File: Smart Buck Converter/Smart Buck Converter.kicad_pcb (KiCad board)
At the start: 2 copper layers, 80 x 45 mm, 73 parts, among them J1 691101710003, J2 PJ-063AH, J3 USB4105-GF-A, J4 PJ-063AH, J6 PJ-063AH, Q1 IRFR9220TRPBF-BE3, U1 LM2596S-ADJ, U2 ATSAMD21E18A-A, U3 AP2204K-3.3, U4 INA219AxD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

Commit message: Changes to README & Design
Updated revision number of hardware design to 2.0.0, despite the changes for this revision being implemented before this project was version controlled on GitHub. Also regenerated 3D view images of revision 2 and replaced them in the README. Added detail regarding known hardware bug in README.
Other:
- board text added: "Intelligent DC-DC Converter 04/2023 V2.0.0"
- board text removed: "Intelligent DC-DC Converter 03/2023 V1.0.0"

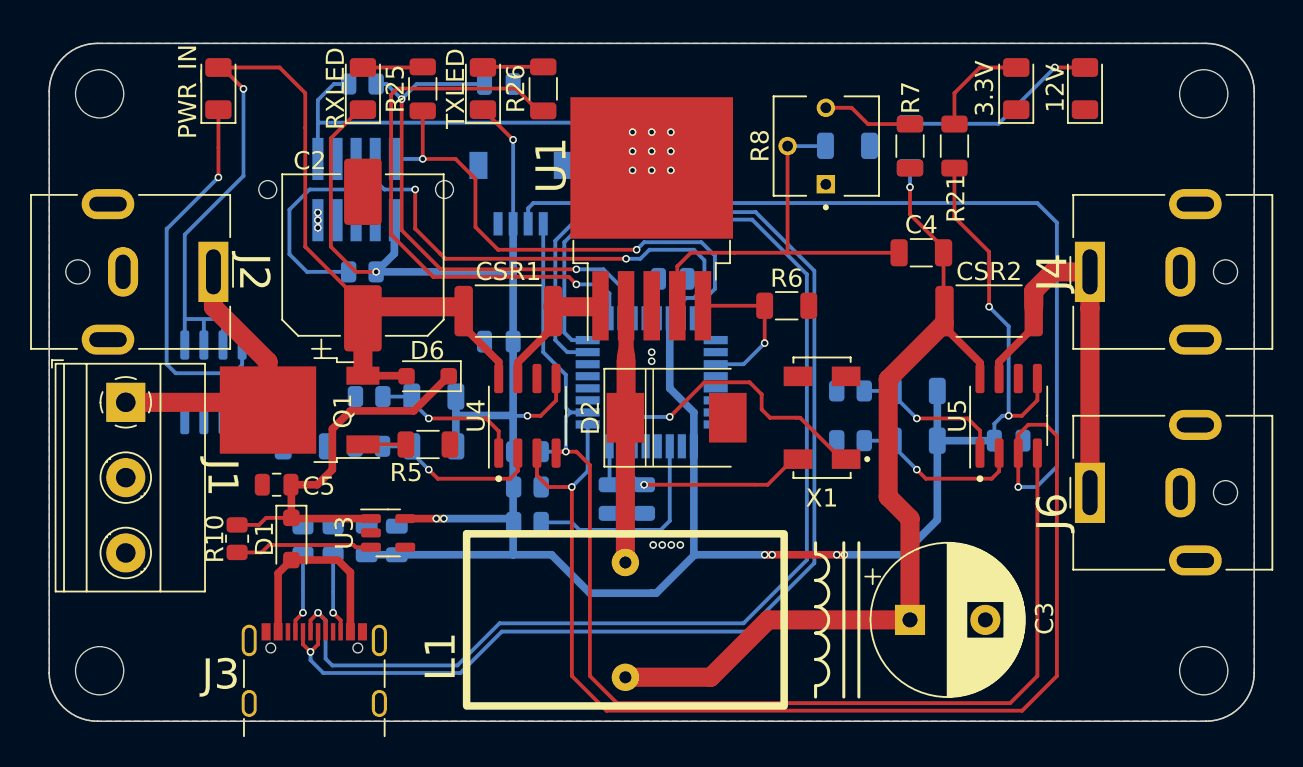
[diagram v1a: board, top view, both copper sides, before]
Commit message: Revision 2 update
Regenerated gerber files to rev 2 design, made minor changes to PCB layout before exporting. Changed I2C interface connector from 4-pin right angle style to vertical style, added the new connector the the KiCad footprints library.
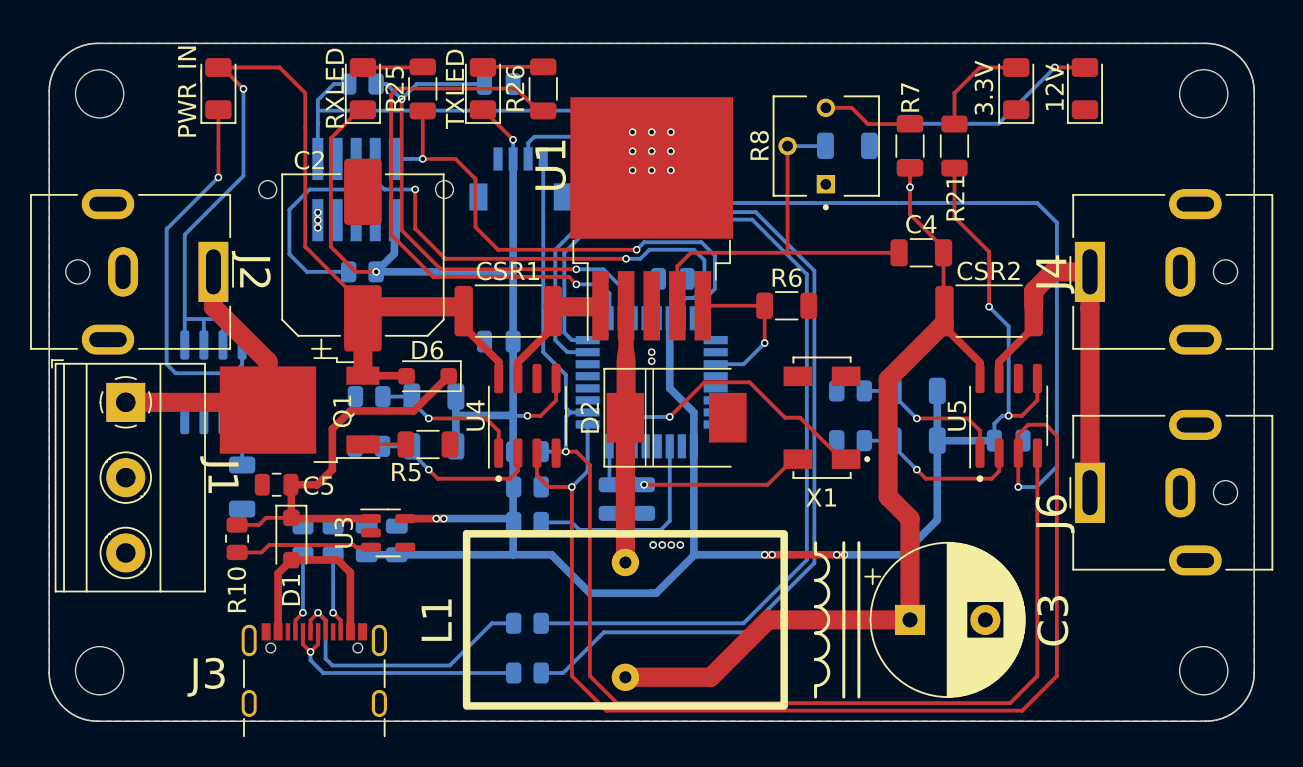
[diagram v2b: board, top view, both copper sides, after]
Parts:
- added R27: 0, Resistor_SMD:R_0805_2012Metric, B.Cu at (31.8, 39.3)
- added R28: 0, Resistor_SMD:R_0805_2012Metric, B.Cu at (31.8, 36.0)
- D1, D6: value PMEG3015EH -> CDBMHT340-HF
- I^{2}C: footprint User Components:JST_SM04B-SRSS-TB(LF)(SN) -> User Components:CONN_BM04B-SRSS-TBT(LF)(SN)
- moved R22 4.98 mm to (12.8, 27.0), turned to -90 degrees
- moved I^{2}C 4.30 mm to (31.3, 5.17)
- moved RESET 0.80 mm to (40.0, 3.86)
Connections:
- U2 pad 23: USB_D- -> (no net)
- U2 pad 24: USB_D+ -> (no net)
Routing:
- net USB_D-: track 88.5 -> 17.5 mm
- net Net-(U2-PA24): track 0.00 -> 68.9 mm
- net USB_D+: track 86.2 -> 20.0 mm
- net Net-(U2-PA25): track 0.00 -> 63.9 mm
- net I^{2}C.SCL: track 81.3 -> 85.6 mm
- net I^{2}C.SDA: track 136.1 -> 139.9 mm
- net /Current Monitoring/PWR_OUT_IMON+: track 56.8 -> 58.1 mm
- net Net-(U6-FB): track 4.16 -> 3.01 mm
- net Net-(U2-PA15): track 23.3 -> 22.7 mm
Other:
- board text added: "I^{2}C ADDR"
- board text added: "Intelligent DC-DC Converter 06/2023 V2.0.0"
- board text removed: "Intelligent DC-DC Converter 04/2023 V2.0.0"
